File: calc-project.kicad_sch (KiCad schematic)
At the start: 39 parts, among them J1 PinSocket_1x20_Right, J2 PinSocket_1x20_Left, J3 Conn_01x14, SW1 SW_Push_45deg, SW10 SW_Push_45deg, SW11 SW_Push_45deg, SW12 SW_Push_45deg, SW13 SW_Push_45deg, SW14 SW_Push_45deg, SW15 SW_Push_45deg, SW16 SW_Push_45deg, SW17 SW_Push_45deg, SW18 SW_Push_45deg, SW19 SW_Push_45deg, SW2 SW_Push_45deg, SW20 SW_Push_45deg, SW21 SW_Push_45deg, SW22 SW_Push_45deg, SW23 SW_Push_45deg, SW24 SW_Push_45deg, SW25 SW_Push_45deg, SW26 SW_Push_45deg, SW27 SW_Push_45deg, SW28 SW_Push_45deg, SW29 SW_Push_45deg, SW3 SW_Push_45deg, SW30 SW_Push_45deg, SW31 SW_Push_45deg, SW32 SW_Push_45deg, SW33 SW_Push_45deg, SW34 SW_Push_45deg, SW35 SW_Push_45deg, SW36 SW_Push_45deg, SW4 SW_Push_45deg, SW5 SW_Push_45deg, SW6 SW_Push_45deg, SW7 SW_Push_45deg, SW8 SW_Push_45deg, SW9 SW_Push_45deg

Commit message: random stuff, i think it helps
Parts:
- added H1, H2, H3, H4, H5: MountingHole, MountingHole:MountingHole_2.1mm, symbol Mechanical:MountingHole
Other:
- note added: "mounting holes"

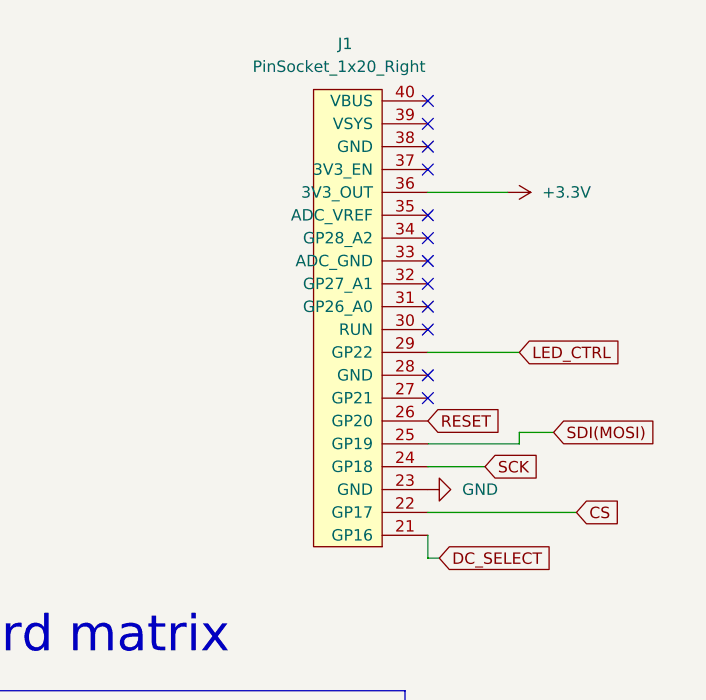
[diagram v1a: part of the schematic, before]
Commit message: replaced old headers, now new ones
also took out routing for rows
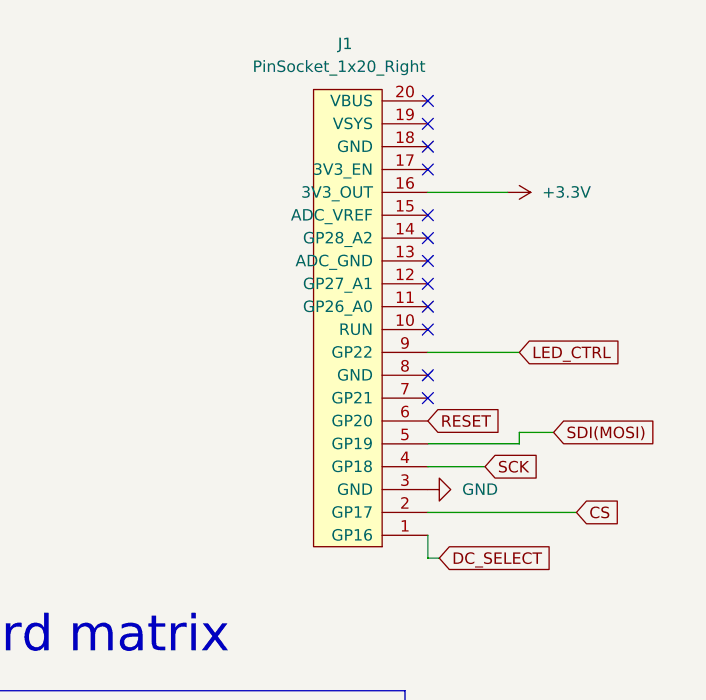
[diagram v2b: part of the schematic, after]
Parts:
- J1, J2: footprint Connector_PinSocket_2.54mm:PinSocket_1x20_P2.54mm_Vertical_SMD_Pin1Left -> Connector_PinSocket_2.54mm:PinSocket_1x20_P2.54mm_Vertical
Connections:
- net +3.3V: now also J1.16 (3V3_OUT); no longer J1.36 (3V3_OUT)
- net CS: now also J1.2 (GP17); no longer J1.22 (GP17)
- net DC_SELECT: now also J1.1 (GP16); no longer J1.21 (GP16)
- net GND: now also J1.3 (GND); no longer J1.23 (GND)
- net LED_CTRL: now also J1.9 (GP22); no longer J1.29 (GP22)
- net RESET: now also J1.6 (GP20); no longer J1.26 (GP20)
- net SCK: now also J1.4 (GP18); no longer J1.24 (GP18)
- net SDI(MOSI): now also J1.5 (GP19); no longer J1.25 (GP19)
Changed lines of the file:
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@@
 			)
 		)
-		(property "Footprint" "Connector_PinSocket_2.54mm:PinSocket_1x20_P2.54mm_Vertical_SMD_Pin1Left"
+		(property "Footprint" "Connector_PinSocket_2.54mm:PinSocket_1x20_P2.54mm_Vertical"
 			(at 173.99 45.72 0)
 			(hide yes)
@@
 			)
 		)
-		(property "Footprint" "Connector_PinSocket_2.54mm:PinSocket_1x20_P2.54mm_Vertical_SMD_Pin1Left"
+		(property "Footprint" "Connector_PinSocket_2.54mm:PinSocket_1x20_P2.54mm_Vertical"
 			(at 231.14 45.72 0)
 			(hide yes)
@@
 			)
 		)
-		(pin "38"
-		)
-		(pin "26"
-		)
-		(pin "33"
-		)
-		(pin "23"
-		)
-		(pin "28"
-		)
-		(pin "36"
-		)
-		(pin "37"
-		)
-		(pin "30"
-		)
-		(pin "31"
-		)
-		(pin "22"
-		)
-		(pin "35"
-		)
-		(pin "21"
-		)
-		(pin "24"
-		)
-		(pin "25"
-		)
-		(pin "29"
-		)
-		(pin "32"
-		)
-		(pin "34"
-		)
-		(pin "27"
-		)
-		(pin "39"
-		)
-		(pin "40"
-		)
-		(instances
+		(pin "3"
+		)
+		(pin "18"
+		)
+		(pin "1"
+		)
+		(pin "6"
+		)
+		(pin "2"
+		)
+		(pin "9"
+		)
+		(pin "11"
+		)
+		(pin "13"
+		)
+		(pin "10"
+		)
+		(pin "15"
+		)
+		(pin "16"
+		)
+		(pin "14"
+		)
+		(pin "8"
+		)
+		(pin "12"
+		)
+		(pin "17"
+		)
+		(pin "4"
+		)
+		(pin "19"
+		)
+		(pin "5"
+		)
+		(pin "20"
+		)
+		(pin "7"
+		)
+		(instances
